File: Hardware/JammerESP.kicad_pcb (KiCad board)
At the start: 2 copper layers, 50 x 100 mm, 19 parts, among them J1 NRF24L01, J2 NRF24L01, J3 Conn_01x03_Socket, SW1 UP, SW2 DOWN, SW3 LEFT, SW4 RIGHT, U1 ESP32-DEVKIT-V1, U2 DM-OLED096-636, U3 AMS1117-3.3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

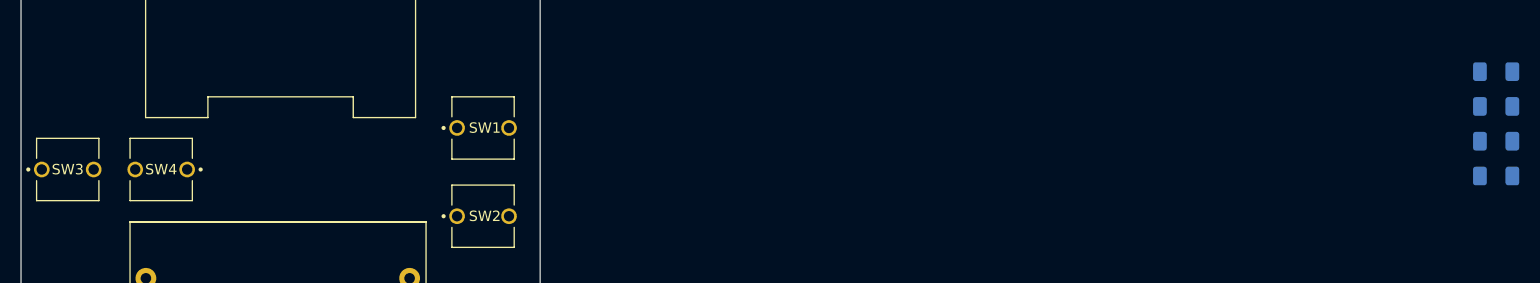
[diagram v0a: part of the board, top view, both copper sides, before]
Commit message: feat: put capacitors and check battery dimension
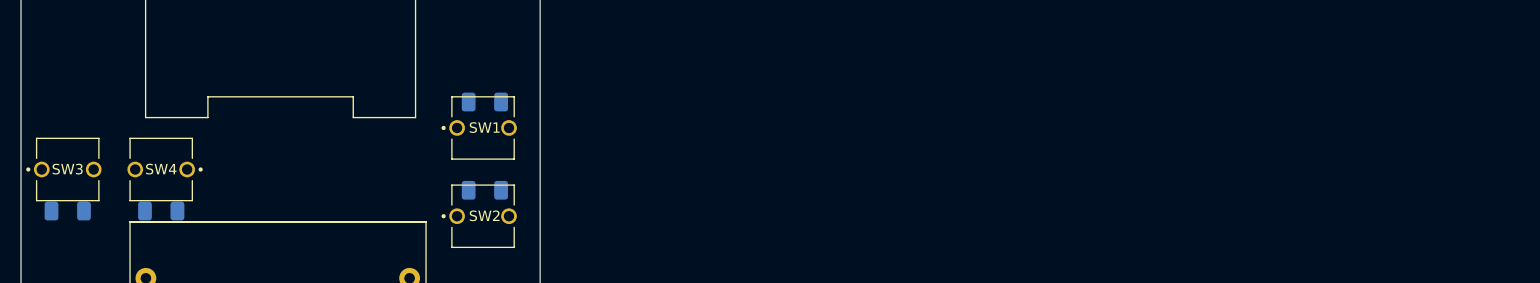
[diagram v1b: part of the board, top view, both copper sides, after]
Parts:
- moved C7 137.7 mm to (69.0, 96.5), turned to 0 degrees
- moved C8 128.6 mm to (78.0, 96.5)
- moved C6 97.7 mm to (109.2, 94.5)
- moved C5 97.4 mm to (109.2, 86.0), turned to 0 degrees
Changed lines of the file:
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@@
 	(footprint "Capacitor_SMD:C_1206_3216Metric_Pad1.33x1.80mm_HandSolder"
 		(layer "B.Cu")
-		(at 206.57238 86.425 180)
+		(at 109.175 94.5 180)
 		(descr "Capacitor SMD 1206 (3216 Metric), square (rectangular) end terminal, IPC-7351 nominal with elongated pad for handsoldering. (Body size source: IPC-SM-782 page 76, https://www.pcb-3d.com/wordpress/wp-content/uploads/ipc-sm-782a_amendment_1_and_2.pdf)")
 		(tags "capacitor handsolder")
 		(property "Reference" "C6"
-			(at 0 1.85 0)
+			(at 97.63488 1.925 180)
 			(layer "B.SilkS")
 			(effects
@@
 	(footprint "Capacitor_SMD:C_1206_3216Metric_Pad1.33x1.80mm_HandSolder"
 		(layer "B.Cu")
-		(at 206.57238 89.775 180)
+		(at 69 96.5)
 		(descr "Capacitor SMD 1206 (3216 Metric), square (rectangular) end terminal, IPC-7351 nominal with elongated pad for handsoldering. (Body size source: IPC-SM-782 page 76, https://www.pcb-3d.com/wordpress/wp-content/uploads/ipc-sm-782a_amendment_1_and_2.pdf)")
 		(tags "capacitor handsolder")
@@
 		(duplicate_pad_numbers_are_jumpers no)
 		(fp_line
+			(start -0.711252 -0.91)
+			(end 0.711252 -0.91)
+			(stroke
+				(width 0.12)
+				(type solid)
+			)
+			(layer "B.SilkS")
+		)
+		(fp_line
 			(start -0.711252 0.91)
 			(end 0.711252 0.91)
-			(stroke
-				(width 0.12)
-				(type solid)
-			)
-			(layer "B.SilkS")
-		)
-		(fp_line
-			(start -0.711252 -0.91)
-			(end 0.711252 -0.91)
 			(stroke
 				(width 0.12)
@@
 		)
 		(pad "1" smd roundrect
-			(at -1.5625 0 180)
+			(at -1.5625 0)
 			(size 1.325 1.8)
 			(layers "B.Cu" "B.Mask" "B.Paste")
@@
 		)
 		(pad "2" smd roundrect
-			(at 1.5625 0 180)
+			(at 1.5625 0)
 			(size 1.325 1.8)
 			(layers "B.Cu" "B.Mask" "B.Paste")
@@
 	(footprint "Capacitor_SMD:C_1206_3216Metric_Pad1.33x1.80mm_HandSolder"
 		(layer "B.Cu")
-		(at 206.57238 83.075 180)
+		(at 109.175 86)
 		(descr "Capacitor SMD 1206 (3216 Metric), square (rectangular) end terminal, IPC-7351 nominal with elongated pad for handsoldering. (Body size source: IPC-SM-782 page 76, https://www.pcb-3d.com/wordpress/wp-content/uploads/ipc-sm-782a_amendment_1_and_2.pdf)")
 		(tags "capacitor handsolder")
@@
 		(duplicate_pad_numbers_are_jumpers no)
 		(fp_line
+			(start -0.711252 -0.91)
+			(end 0.711252 -0.91)
+			(stroke
+				(width 0.12)
+				(type solid)
+			)
+			(layer "B.SilkS")
+		)
+		(fp_line
 			(start -0.711252 0.91)
 			(end 0.711252 0.91)
-			(stroke
-				(width 0.12)
-				(type solid)
-			)
-			(layer "B.SilkS")
-		)
-		(fp_line
-			(start -0.711252 -0.91)
-			(end 0.711252 -0.91)
 			(stroke
 				(width 0.12)
@@
 		)
 		(pad "1" smd roundrect
-			(at -1.5625 0 180)
+			(at -1.5625 0)
 			(size 1.325 1.8)
 			(layers "B.Cu" "B.Mask" "B.Paste")
@@
 		)
 		(pad "2" smd roundrect
-			(at 1.5625 0 180)
+			(at 1.5625 0)
 			(size 1.325 1.8)
 			(layers "B.Cu" "B.Mask" "B.Paste")
@@
 	(footprint "Capacitor_SMD:C_1206_3216Metric_Pad1.33x1.80mm_HandSolder"
 		(layer "B.Cu")
-		(at 206.57238 93.125 180)
+		(at 78 96.5 180)
 		(descr "Capacitor SMD 1206 (3216 Metric), square (rectangular) end terminal, IPC-7351 nominal with elongated pad for handsoldering. (Body size source: IPC-SM-782 page 76, https://www.pcb-3d.com/wordpress/wp-content/uploads/ipc-sm-782a_amendment_1_and_2.pdf)")
 		(tags "capacitor handsolder")
@@
 		)
 	)
+	(gr_rect
+		(start 121.5 46)
+		(end 151.5 96)
+		(stroke
+			(width 0.1)
+			(type solid)
+		)
+		(fill no)
+		(layer "Dwgs.User")
+	)
 	(gr_line

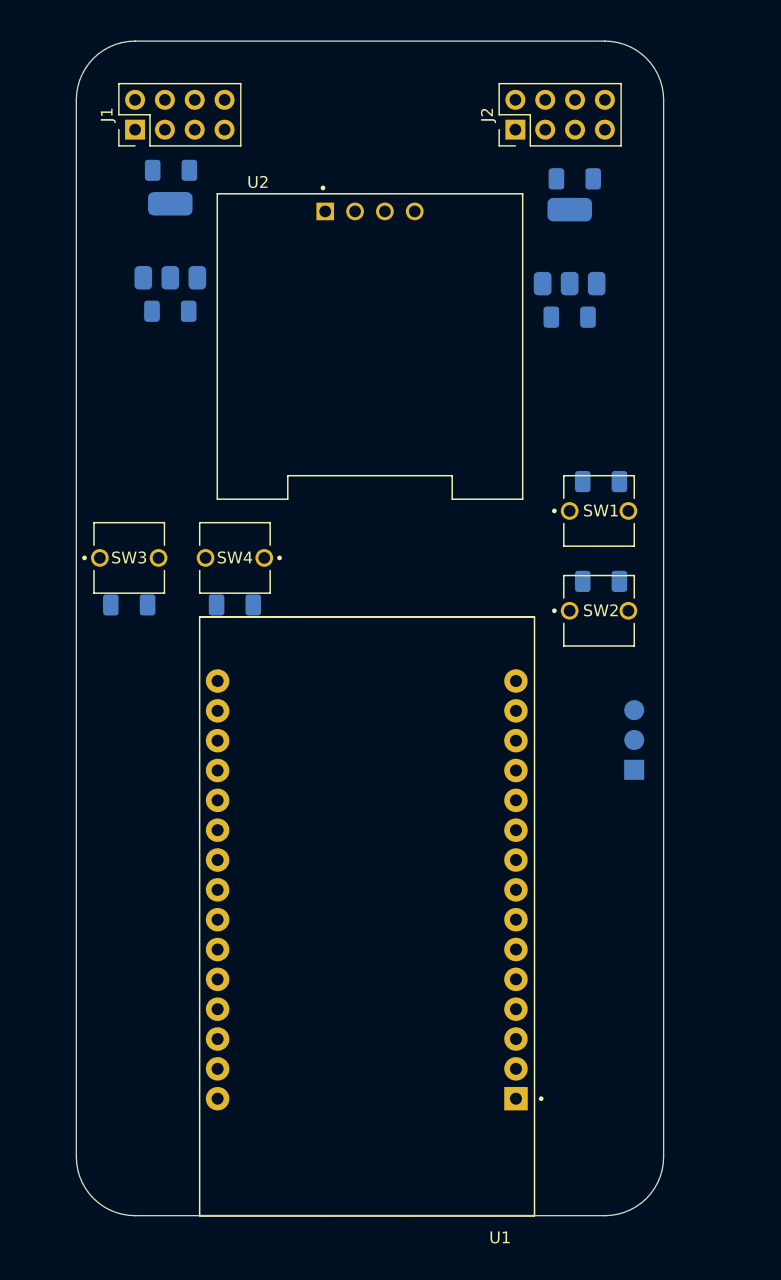
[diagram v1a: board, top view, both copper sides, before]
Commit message: Add routes
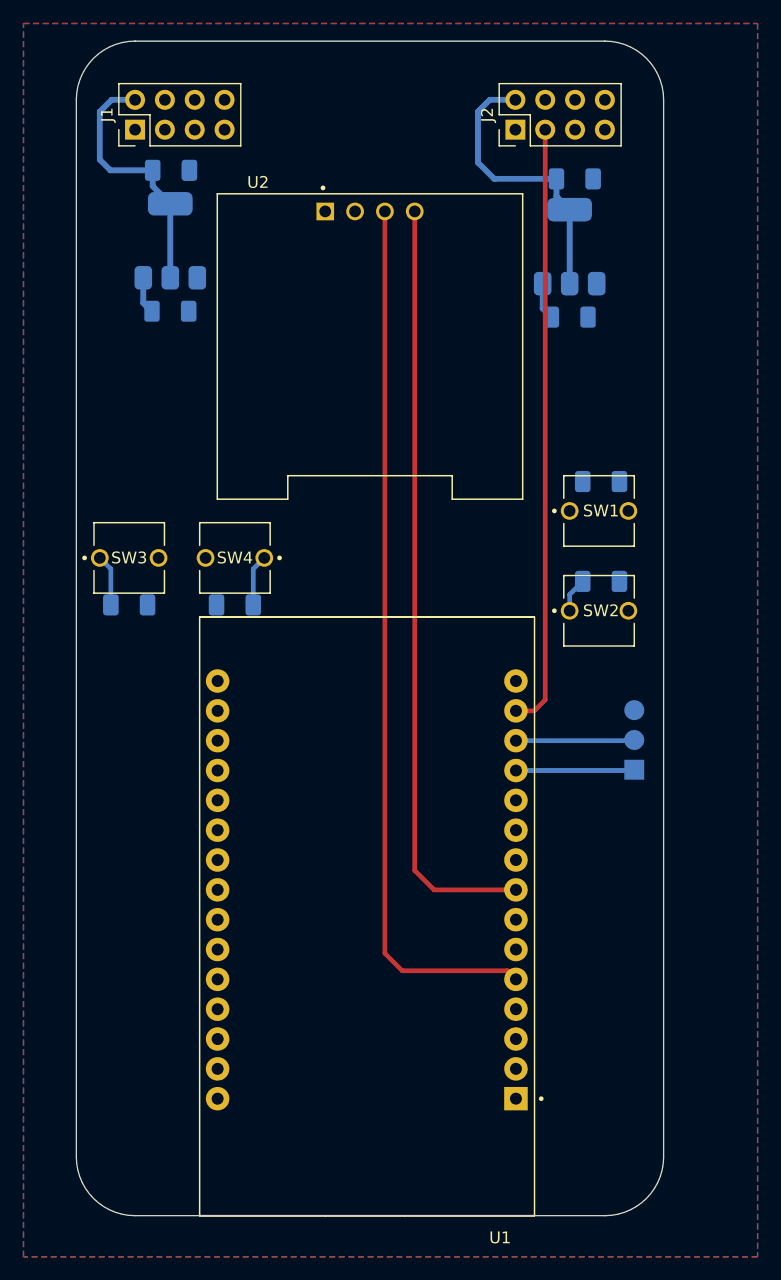
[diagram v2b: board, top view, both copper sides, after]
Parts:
- turned C3 to 0 degrees
- turned C6 to 0 degrees
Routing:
- net /SCL: track 0.00 -> 75.2 mm
- net /SDA: track 0.00 -> 65.4 mm
- net /V_CE: track 0.00 -> 51.4 mm
- net VCC_NRF2: track 0.00 -> 24.6 mm
- net VCC_NRF1: track 0.00 -> 22.2 mm
- net Net-(J3-Pin_2): track 0.00 -> 10.1 mm
- net Net-(J3-Pin_1): track 0.00 -> 10.1 mm
- net +5V: track 0.00 -> 6.33 mm
- net /RIGHT: track 0.00 -> 4.39 mm
- net /LEFT: track 0.00 -> 4.39 mm
- net /DOWN: track 0.00 -> 2.96 mm
- added copper zone on B.Cu, net GND
- added copper zone on F.Cu, net GND

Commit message: update routes
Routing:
- net /H_MOSI: track 0.00 -> 97.6 mm
- net /H_CS: track 0.00 -> 88.3 mm
- net +3V3_ESP: track 0.00 -> 88.2 mm
- net /H_MISO: track 0.00 -> 83.0 mm
- net /H_CLK: track 0.00 -> 78.2 mm
- net /H_CE: track 0.00 -> 69.7 mm
- net /V_CLK: track 0.00 -> 68.0 mm
- net /V_MISO: track 0.00 -> 66.3 mm, vias 0 -> 1
- net /SCL: track 75.2 -> 74.0 mm
- net /SDA: track 65.4 -> 64.5 mm
- net GND: vias 0 -> 26
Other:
- outline, holes or cut-outs redrawn

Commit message: update routes
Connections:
- U1 pad 21: /DOWN -> /UP
- U1 pad 23: /UP -> /DOWN
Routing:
- net +5V: track 6.33 -> 119.9 mm, vias 0 -> 2
- net /V_CS: track 0.00 -> 70.8 mm
- net /V_MOSI: track 0.00 -> 69.3 mm, vias 0 -> 2
- net /UP: track 0.00 -> 58.7 mm
- net /DOWN: track 2.96 -> 55.3 mm
- net /LEFT: track 4.39 -> 34.5 mm
- net /RIGHT: track 4.39 -> 23.4 mm
- net GND: vias 26 -> 32
